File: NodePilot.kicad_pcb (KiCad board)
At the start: 2 copper layers, 100 x 70 mm, 51 parts, among them K1 SRD-05VDC-SL-C, Q1 2N3904, Q2 2N2222, Q4 2N3904, T1 1:1 600R, T2 1:1 600R, U1 PC817, U2 PC817, U3 B0505S-1WR2

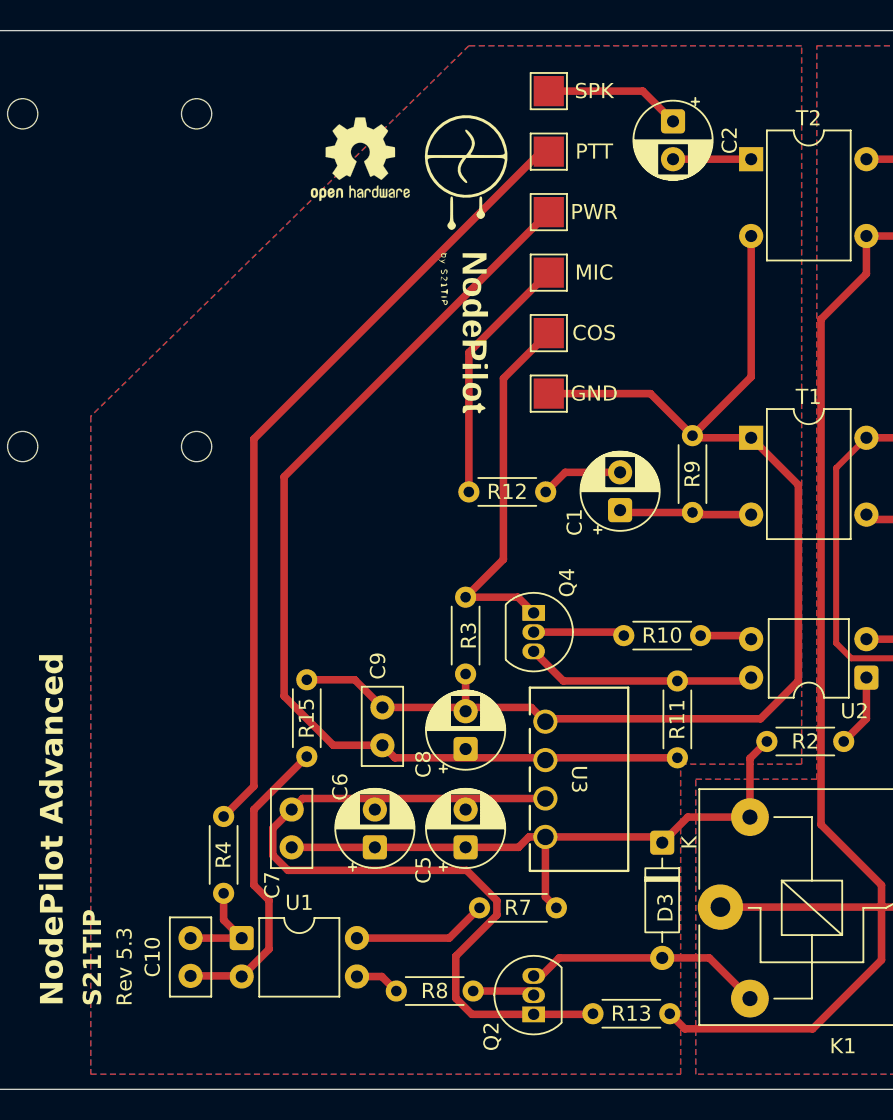
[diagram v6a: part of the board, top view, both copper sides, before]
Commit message: fix for GP zones
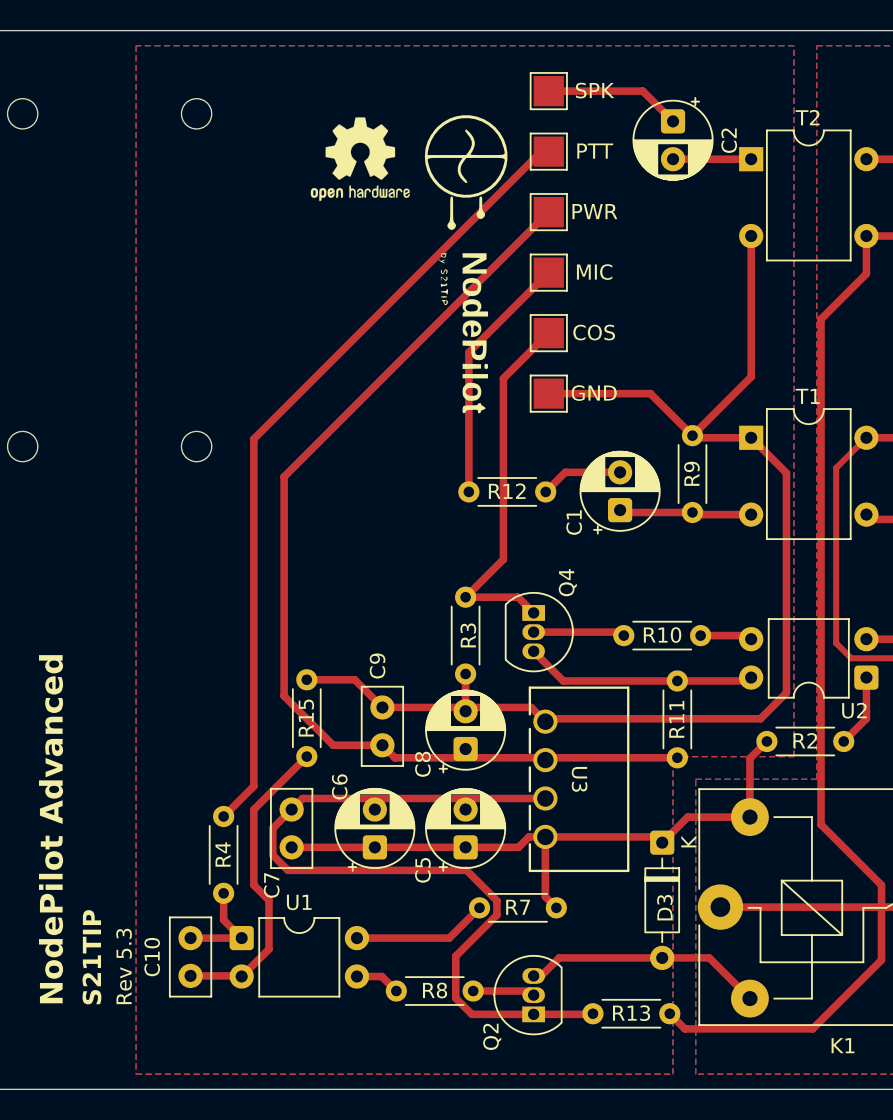
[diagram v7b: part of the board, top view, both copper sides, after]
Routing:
- net GROUND: track 84.5 -> 83.8 mm
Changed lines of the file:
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@@
 		(capping no)
 		(filling no)
-		(zone_defaults)
 		(pcbplotparams
 			(layerselection 0x00000000_00000000_55555555_5755f5ff)
@@
 	)
 	(segment
-		(start 164.285113 110)
-		(end 166.785113 107.5)
-		(width 0.5)
-		(layer "F.Cu")
-		(net "GROUND")
-	)
-	(segment
 		(start 163.525113 91.28)
 		(end 163.665113 91.42)
@@
 	)
 	(segment
-		(start 150.250113 110)
-		(end 164.285113 110)
-		(width 0.5)
-		(layer "F.Cu")
-		(net "GROUND")
-	)
-	(segment
-		(start 150.060113 110.19)
-		(end 150.250113 110)
+		(start 166 93.754887)
+		(end 163.665113 91.42)
 		(width 0.5)
 		(layer "F.Cu")
@@
 	)
 	(segment
-		(start 166.785113 107.5)
-		(end 166.785113 94.54)
+		(start 164.285113 110)
+		(end 166 108.285113)
 		(width 0.5)
 		(layer "F.Cu")
@@
 	)
 	(segment
+		(start 166 108.285113)
+		(end 166 93.754887)
+		(width 0.5)
+		(layer "F.Cu")
+		(net "GROUND")
+	)
+	(segment
 		(start 137.455113 107.42)
 		(end 139.285113 109.25)
@@
 	)
 	(segment
+		(start 150.060113 110.19)
+		(end 150.250113 110)
+		(width 0.5)
+		(layer "F.Cu")
+		(net "GROUND")
+	)
+	(segment
 		(start 134.285113 107.42)
 		(end 137.455113 107.42)
@@
 	)
 	(segment
-		(start 157.005113 88.5)
-		(end 150.285113 88.5)
+		(start 150.250113 110)
+		(end 164.285113 110)
 		(width 0.5)
 		(layer "F.Cu")
@@
 	)
 	(segment
-		(start 166.785113 94.54)
-		(end 163.665113 91.42)
+		(start 157.005113 88.5)
+		(end 150.285113 88.5)
 		(width 0.5)
 		(layer "F.Cu")
@@
 		(polygon
 			(pts
-				(xy 167 113) (xy 167 65.5) (xy 145 65.5) (xy 120 90) (xy 120 133.5) (xy 159 133.5) (xy 159 113)
+				(xy 166.5 112.5) (xy 166.5 65.5) (xy 123 65.5) (xy 123 133.5) (xy 158.5 133.5) (xy 158.5 112.5)
 			)
 		)

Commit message: power connection trace
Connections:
- ? pad 1: (no net) -> Net-(D3-K)
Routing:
- net Net-(D3-K): track 41.9 -> 72.4 mm
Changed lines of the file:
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@@
 			(remove_unused_layers no)
 			(roundrect_rratio 0.104167)
+			(net "Net-(D3-K)")
 		)
 		(pad "2" thru_hole circle
@@
 		(net "Net-(D3-K)")
 	)
+	(segment
+		(start 163.585113 116.5)
+		(end 167.085113 120)
+		(width 0.5)
+		(layer "B.Cu")
+		(net "Net-(D3-K)")
+	)
+	(segment
+		(start 167.085113 120)
+		(end 192.6675 120)
+		(width 0.5)
+		(layer "B.Cu")
+		(net "Net-(D3-K)")
+	)
